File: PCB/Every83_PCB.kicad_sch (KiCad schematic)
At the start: 34 parts, among them J1 781710004, J7 Conn_02x03_Counter_Clockwise, Q1 MMDT2222A, Q2 DMN24H3D5L, Q4 DMN24H3D5L, Q5 DMN24H3D5L, Q6 DMN24H3D5L, Q7 DMN24H3D5L, Q8 DMN24H3D5L, SW101 KMR2, SW102 KMR2, U1 Core52840, U4 LDL40PU33RY

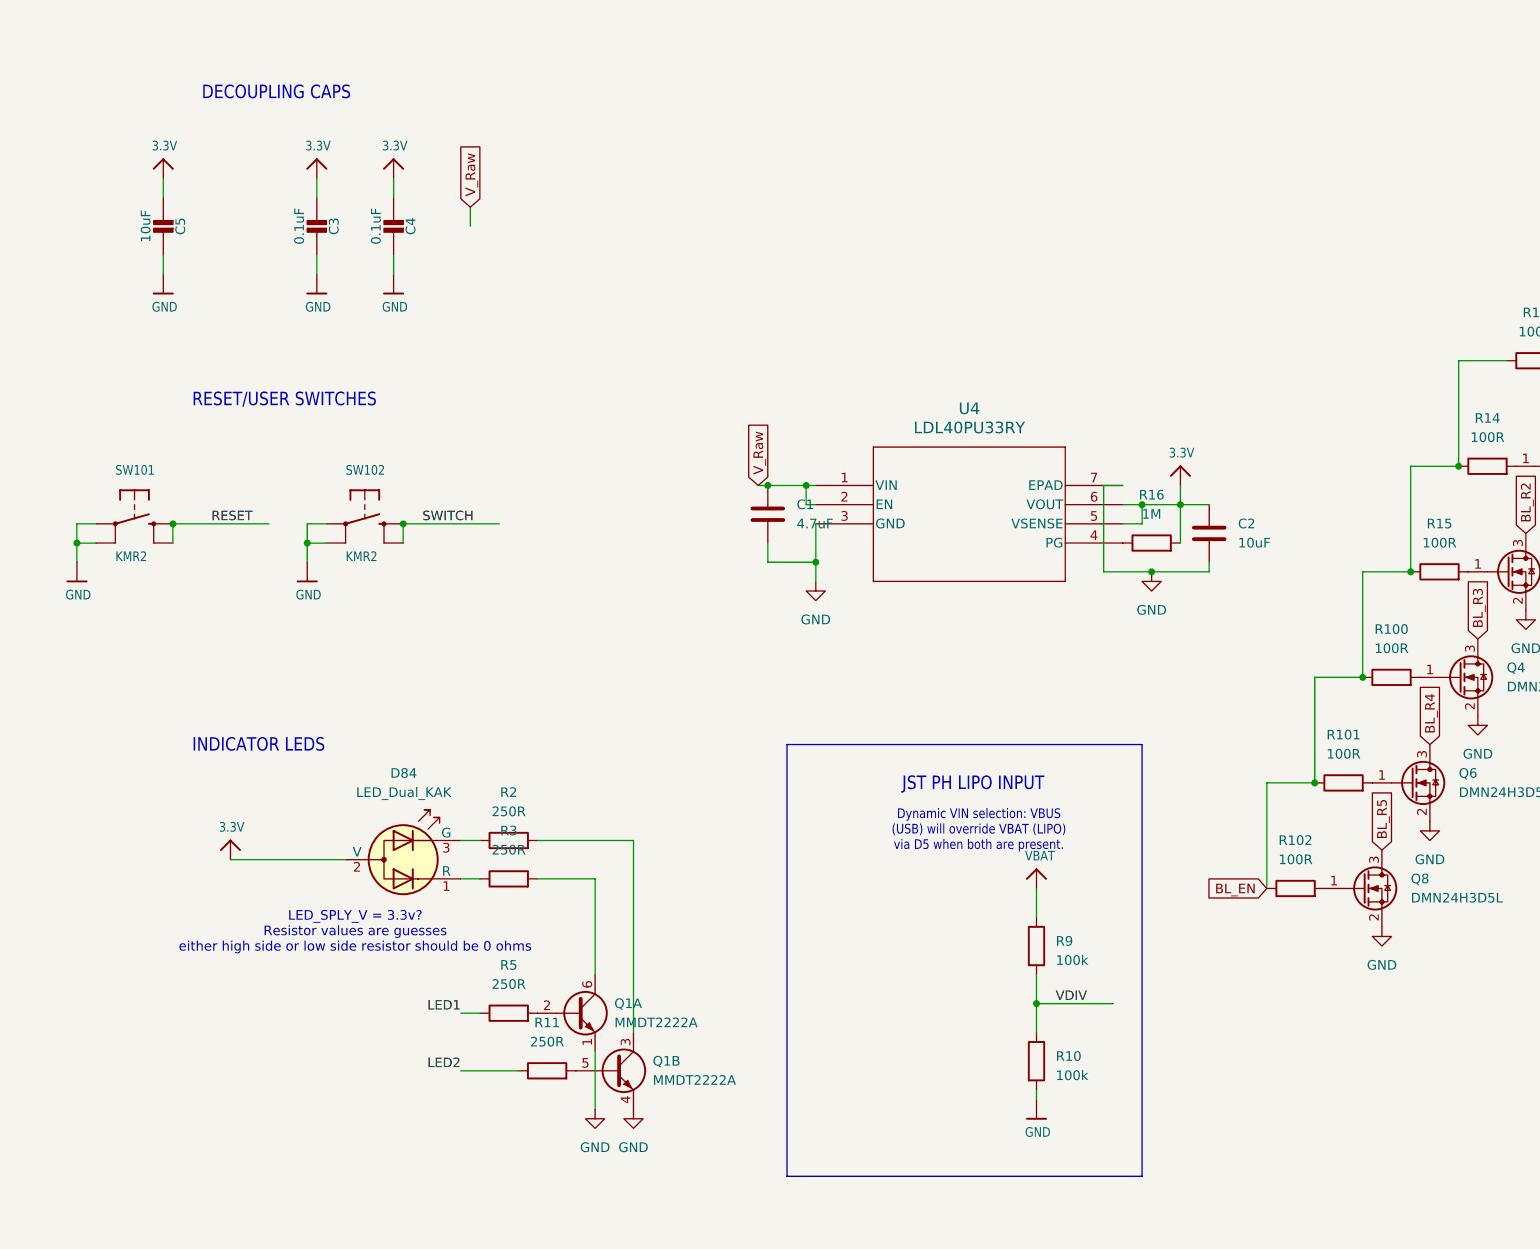
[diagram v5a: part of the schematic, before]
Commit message: Add power switch connector to main board
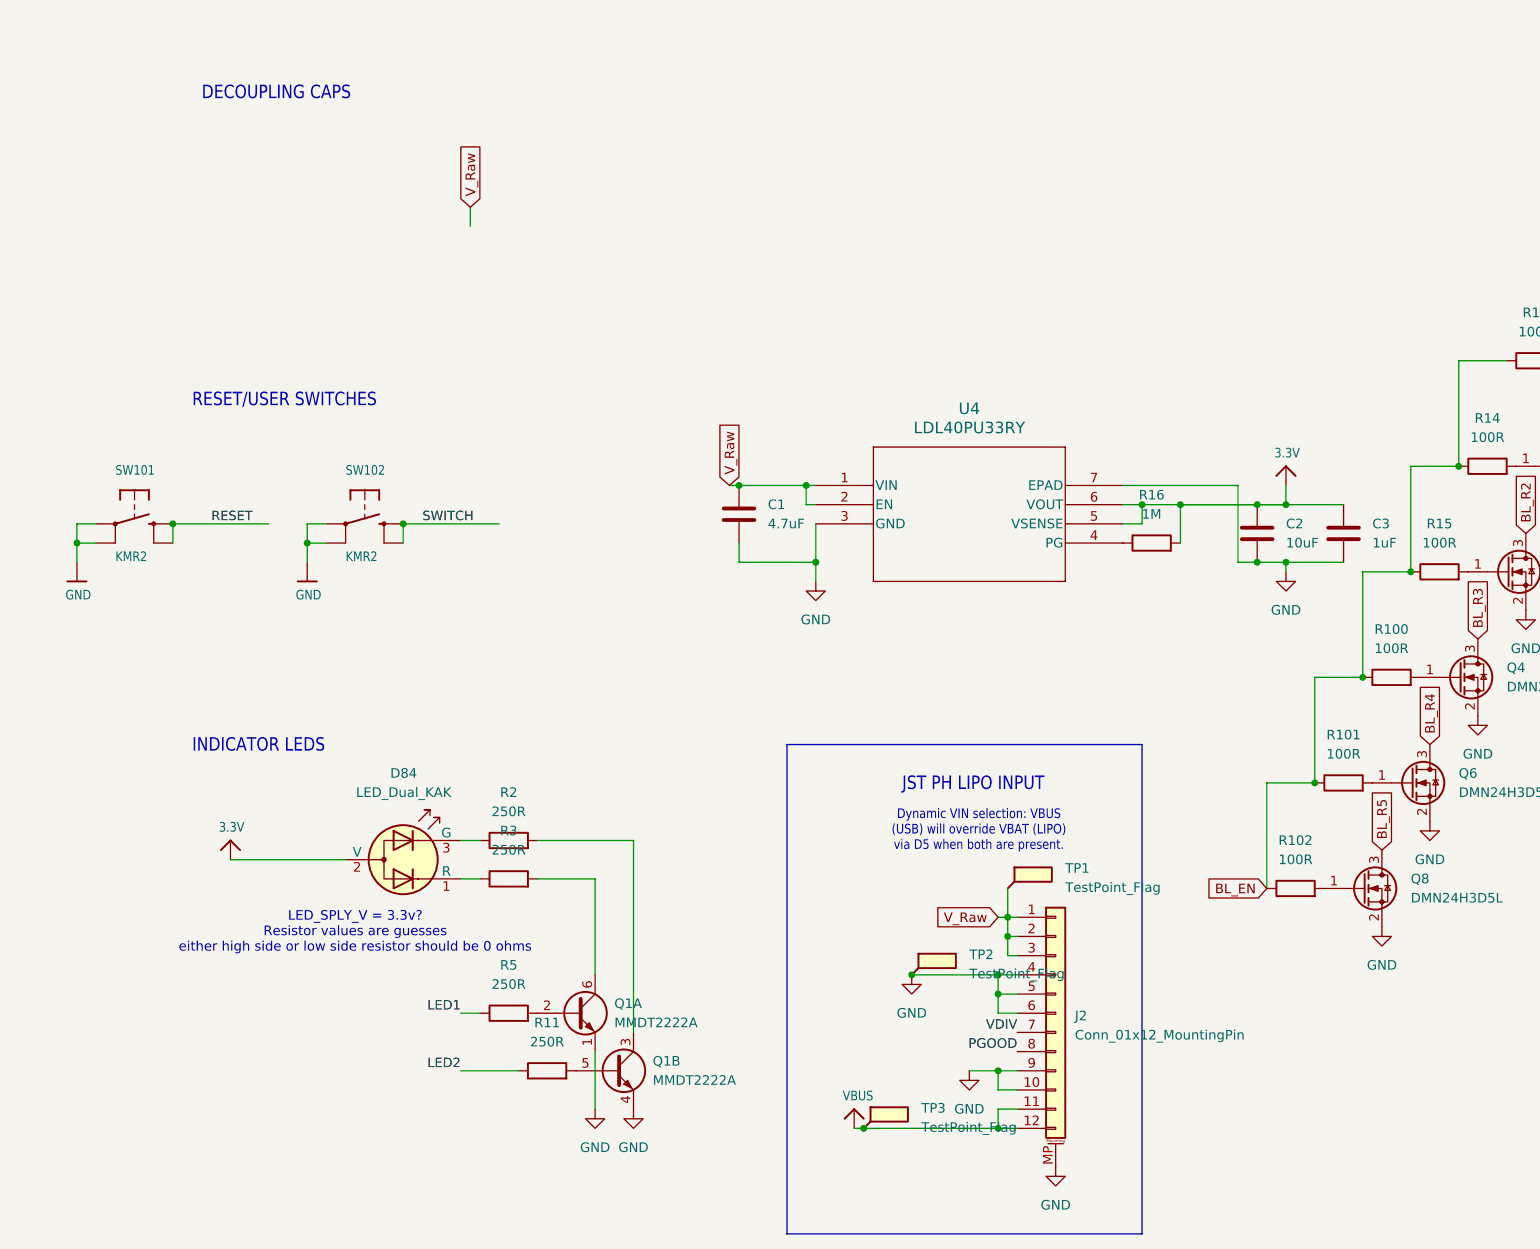
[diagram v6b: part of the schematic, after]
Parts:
- removed C3, C4: 0.1uF, Capacitor_SMD:C_0402_1005Metric, symbol Adafruit nRF52840 Bluefruit Feather Express Rev D-eagle-import:CAP_CERAMIC0603_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
- removed C5: 10uF, Capacitor_SMD:C_0402_1005Metric, symbol Adafruit nRF52840 Bluefruit Feather Express Rev D-eagle-import:CAP_CERAMIC0805-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
- removed R10, R9: 100k, Resistor_SMD:R_0402_1005Metric, symbol Device:R
- added C3: 1uF, Capacitor_SMD:C_0402_1005Metric, symbol Device:C
- added J2: Conn_01x12_MountingPin, GCT_FFC2B28-12-G:GCT_FFC2B28-12-G, symbol Connector_Generic_MountingPin:Conn_01x12_MountingPin
- added TP1, TP2, TP3: TestPoint_Flag, TestPoint:TestPoint_Pad_1.5x1.5mm, symbol Connector:TestPoint_Flag
- C1: footprint Capacitor_SMD:C_0402_1005Metric -> Capacitor_SMD:C_0603_1608Metric; MPN (none) -> GRM188R61E475KE11D
- C2: footprint Capacitor_SMD:C_0402_1005Metric -> Capacitor_SMD:C_0805_2012Metric; MPN (none) -> GRM21BR61H106KE43L
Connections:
- net 3.3V: now also C3.1
- net GND: now also C3.2, J2.10 (Pin_10), J2.4 (Pin_4), J2.5 (Pin_5), J2.6 (Pin_6), J2.9 (Pin_9), J2.MP (MountPin), TP2.1
- net VBUS: now also J2.11 (Pin_11), J2.12 (Pin_12), TP3.1
- net VDIV: now also J2.7 (Pin_7)
- net V_Raw: now also J2.1 (Pin_1), J2.2 (Pin_2), J2.3 (Pin_3), TP1.1
- new net PGOOD: J2.8 (Pin_8)
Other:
- moved on the sheet: C1, C2

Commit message: WIP
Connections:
- net NEOPIX_EN is gone; now on net BL_EN: U1.42 (P1.00)
- net PGOOD: now also U4.2 (EN)
- net V_Raw: no longer U4.2 (EN)
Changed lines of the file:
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@@
-	)
-	(junction
-		(at 124.46 182.88)
-		(diameter 0)
-		(color 0 0 0 0)
 	)
 	(junction
@@
 	(wire
 		(pts
-			(xy 115.57 182.88) (xy 124.46 182.88)
+			(xy 115.57 182.88) (xy 125.73 182.88)
 		)
 		(stroke
@@
 	(wire
 		(pts
-			(xy 124.46 182.88) (xy 125.73 182.88)
-		)
-		(stroke
-			(width 0)
-			(type default)
-		)
-	)
-	(wire
-		(pts
 			(xy 125.73 195.58) (xy 125.73 193.04)
 		)
@@
 	(wire
 		(pts
-			(xy 124.46 185.42) (xy 124.46 182.88)
-		)
-		(stroke
-			(width 0)
-			(type default)
-		)
-	)
-	(wire
-		(pts
 			(xy 125.73 193.04) (xy 125.73 187.96)
 		)
@@
 		(pts
 			(xy 149.86 252.73) (xy 149.86 250.19)
-		)
-		(stroke
-			(width 0)
-			(type default)
-		)
-	)
-	(wire
-		(pts
-			(xy 125.73 185.42) (xy 124.46 185.42)
 		)
 		(stroke
@@
 			)
 			(justify left bottom)
+		)
+	)
+	(label "PGOOD"
+		(at 125.73 185.42 180)
+		(effects
+			(font
+				(size 1.27 1.27)
+			)
+			(justify right bottom)
 		)
 	)
@@
 		)
 	)
-	(global_label "NEOPIX_EN"
-		(shape input)
-		(at 69.85 50.8 0)
-		(fields_autoplaced yes)
-		(effects
-			(font
-				(size 1.27 1.27)
-			)
-			(justify left)
-		)
-		(property "Intersheetrefs" "${INTERSHEET_REFS}"
-			(at 83.1766 50.8 0)
-			(effects
-				(font
-					(size 1.27 1.27)
-				)
-				(justify left)
-				(hide yes)
-			)
-		)
-	)
 	(global_label "Row2"
 		(shape input)
@@
 			(effects
 				(font
+					(size 1.27 1.27)
+				)
+				(justify left)
+				(hide yes)
+			)
+		)
+	)
+	(global_label "BL_EN"
+		(shape input)
+		(at 69.85 50.8 0)
+		(fields_autoplaced yes)
+		(effects
+			(font
+				(size 1.27 1.27)
+			)
+			(justify left)
+		)
+		(property "Intersheetrefs" "${INTERSHEET_REFS}"
+			(at 78.5804 50.8 0)
+			(effects
+				(font

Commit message: WIP
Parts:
- added D101: LED, LED_SMD:LED_1206_3216Metric_ReverseMount_Hole1.8x2.4mm, symbol Device:LED
- added R4: 250R, Resistor_SMD:R_0603_1608Metric, symbol Device:R
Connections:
- net GND: now also R4.1
- net CAPS_LOCK: now reaches U1.43 (P0.22)
- net CAPS_LOCK: now also D101.2 (A)
- new net: D101.1 (K), R4.2
- no-connect marks 1 -> 0
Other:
- note removed: "DECOUPLING CAPS"
- note removed: "Dynamic VIN selection: VBUS (USB) will override VBAT (LIPO) via D5 when both are present."
- note removed: "JST PH LIPO INPUT"
- moved on the sheet: C1, C2, C3, D84, J1, J2, J7, Q1A, Q1B, Q2, Q4, Q5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
